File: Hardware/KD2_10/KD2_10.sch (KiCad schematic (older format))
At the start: 51 parts, among them J1 Conn_01x01, J2 Conn_01x01, J3 Conn_01x06, J4 Conn_01x01, J5 Conn_01x01, J6 Conn_01x01, J7 Conn_01x01, J8 Conn_01x01, J9 dnp, Q1 AO3400A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

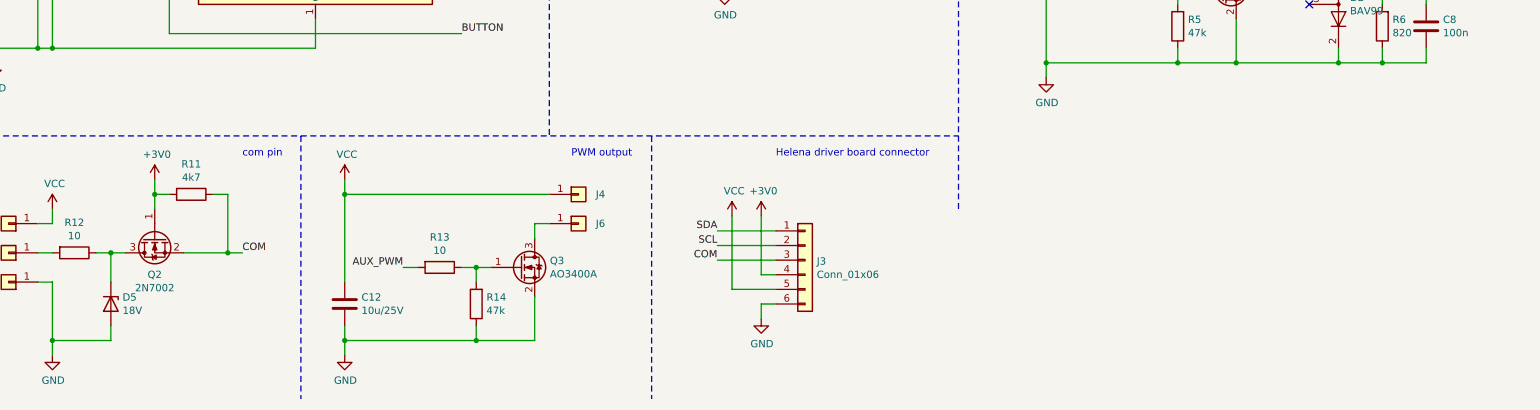
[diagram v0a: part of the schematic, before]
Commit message: documentation update, adaptation to hardware changes
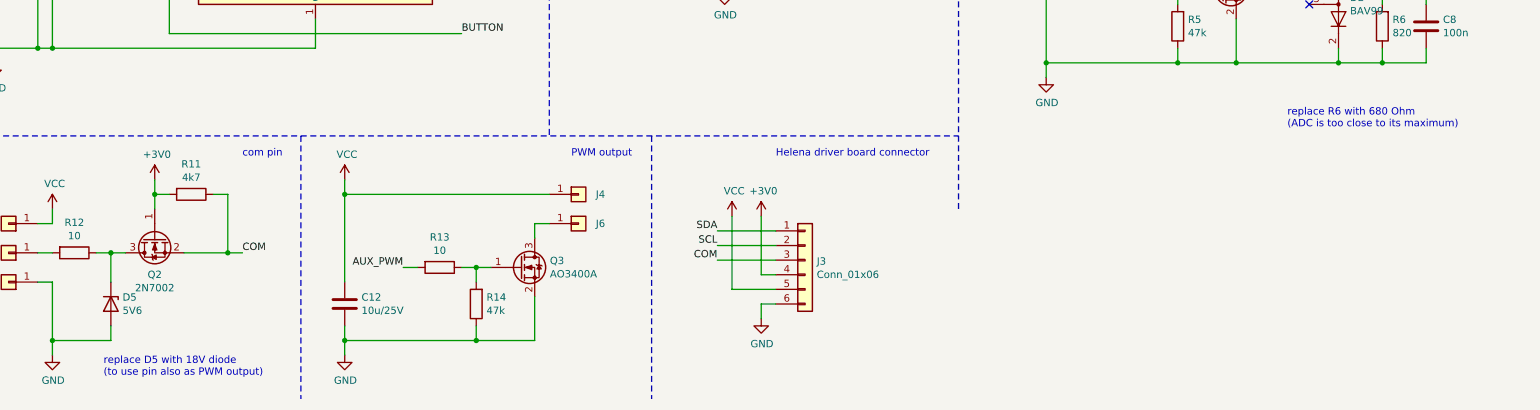
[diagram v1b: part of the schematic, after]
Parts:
- D5: value 18V -> 5V6
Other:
- note added: "replace D5 with 18V diode\n(to use pin also as PWM output)"
- note added: "replace R6 with 680 Ohm\n(ADC is too close to its maximum)"
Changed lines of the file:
@@
 P 1500 7150
 F 0 "D5" V 1454 7230 50  0000 L CNN
-F 1 "18V" V 1545 7230 50  0000 L CNN
+F 1 "5V6" V 1545 7230 50  0000 L CNN
 F 2 "Diode_SMD:D_SOT-23_ANK" H 1500 7150 50  0001 C CNN
 F 3 "~" H 1500 7150 50  0001 C CNN
@@
 Wire Notes Line
 	5500 3800 5300 4500
+Text Notes 1450 7650 0    50   ~ 0
+replace D5 with 18V diode\n(to use pin also as PWM output)
+Text Notes 9550 5950 0    50   ~ 0
+replace R6 with 680 Ohm\n(ADC is too close to its maximum)
 $EndSCHEMATC
